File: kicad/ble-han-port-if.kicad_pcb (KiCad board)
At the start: 2 copper layers, 44.5 x 34.5 mm, 26 parts, among them J1 Conn_01x03, J2 Conn_01x04, J3 Conn_01x06, Q1 BC847, U1 ESP32-C3-WROOM-02-N4, U4 R-78B3.3-1.0 (Recom)

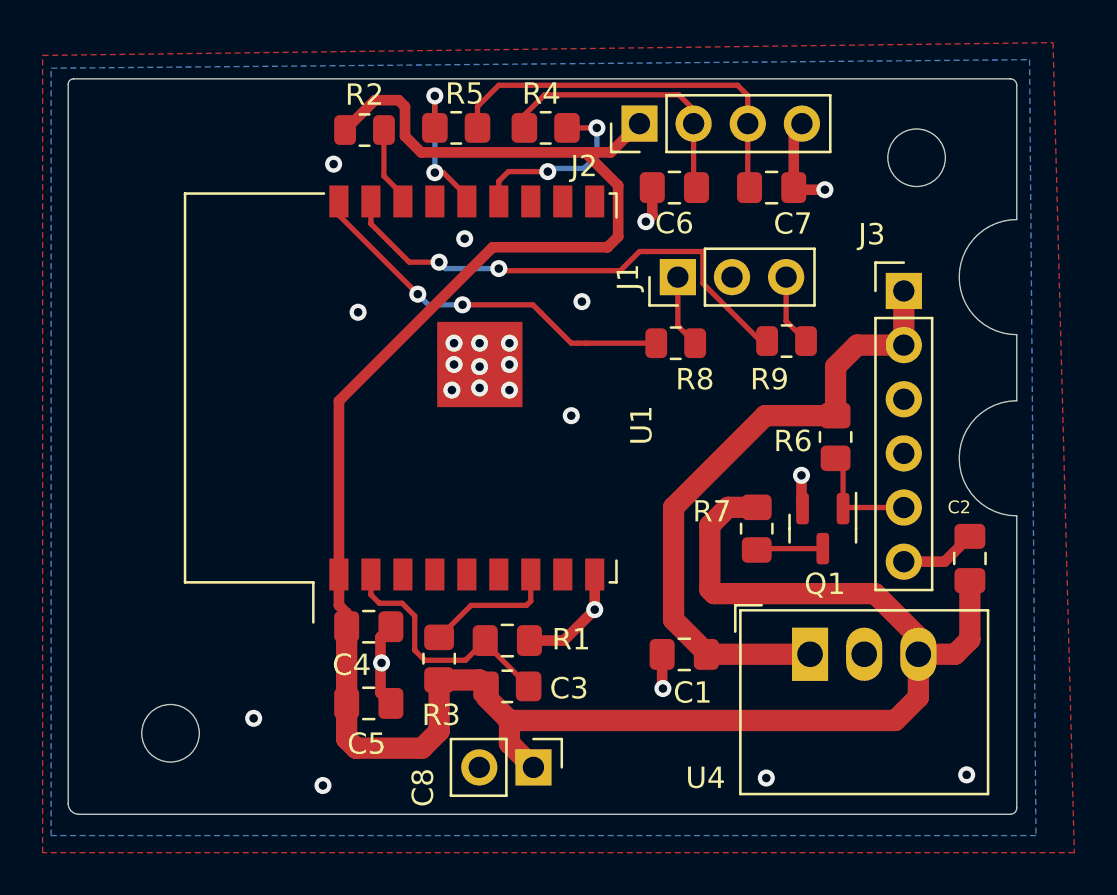
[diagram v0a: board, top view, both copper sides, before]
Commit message: Rerouted USB and fixed pos for holes
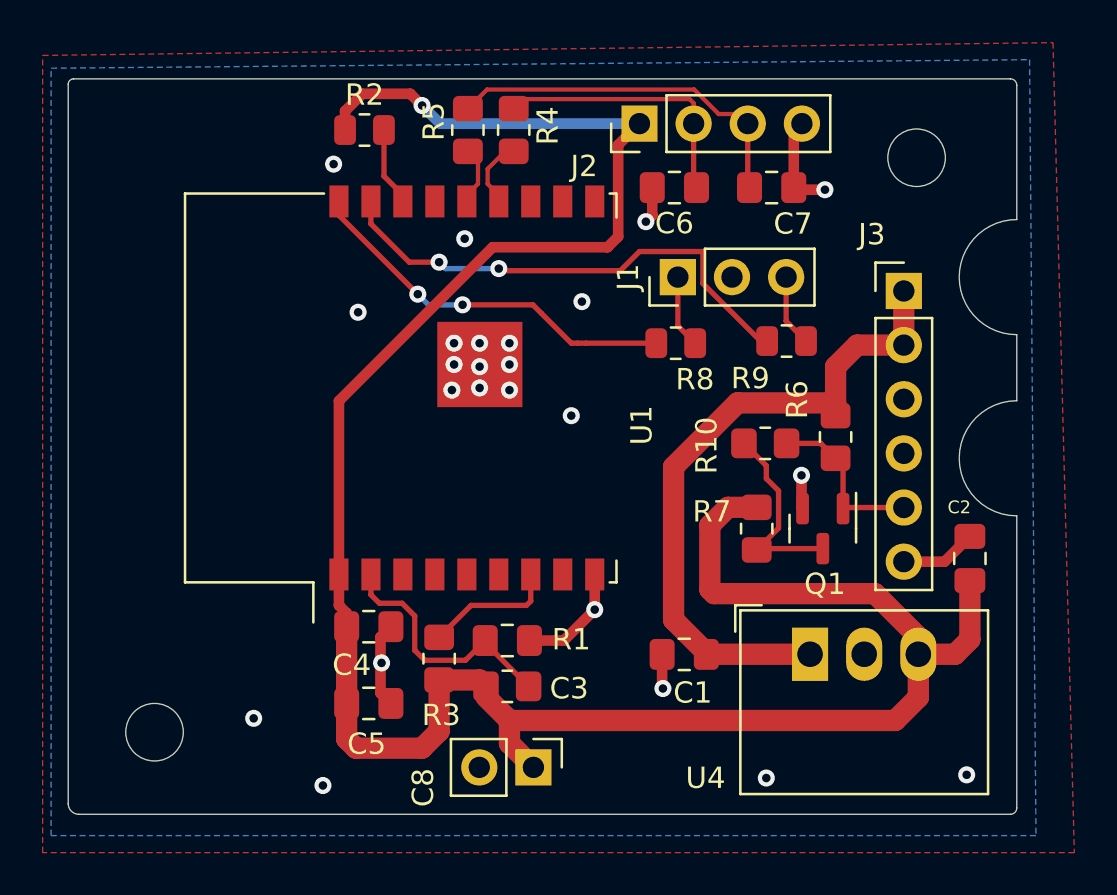
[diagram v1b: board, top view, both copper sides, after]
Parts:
- removed REF**: OSHW-Logo2_14.6x12mm_SilkScreen, Symbol:OSHW-Logo2_14.6x12mm_SilkScreen
- added R10: 0R, Resistor_SMD:R_0805_2012Metric_Pad1.20x1.40mm_HandSolder, F.Cu at (147.9, 101.4)
- moved R4 1.50 mm to (136.1, 86.7), turned to 90 degrees
- moved H1 0.75 mm to (119.2, 115.0)
- moved R5 0.56 mm to (133.9, 86.7), turned to 90 degrees
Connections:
- net Net-(R4-Pad1) renamed /D+
- net Net-(R5-Pad1) renamed /D-
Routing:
- net Net-(Q1-Pad3): track 3.13 -> 9.22 mm
- net /D+: track 8.75 -> 3.31 mm, vias 2 -> 0
- net /D-: track 7.31 -> 2.76 mm, vias 2 -> 0
- net /TX: track 5.38 -> 7.97 mm
- net /USB D+: track 18.6 -> 17.2 mm
- net +5V: track 30.2 -> 31.6 mm
- net +3V3: track 112.2 -> 112.1 mm, vias 0 -> 1
